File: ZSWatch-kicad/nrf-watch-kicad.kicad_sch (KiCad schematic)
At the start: 90 parts, among them IC1 TLV840MAPL36DBVRQ1, IC2 XC9265C181MR-G, IC3 TPS61023DRLT, IC4 MAX30101EFD+T, M1 Vibrator DC Motor, Q1 DMP2045U-7, Q2 SS8050-G, U1 MAX1811ESA+, U2 DMC2400UV-7, U3 LIS2DS12TR, U4 MX25R6435FZNIL0, U5 u-blox ANNA-B402, U6 DRV2603RUNT, U7 XC9265A331MR-G, U8 TXB0104QRUTRQ1, U9 GC9A01

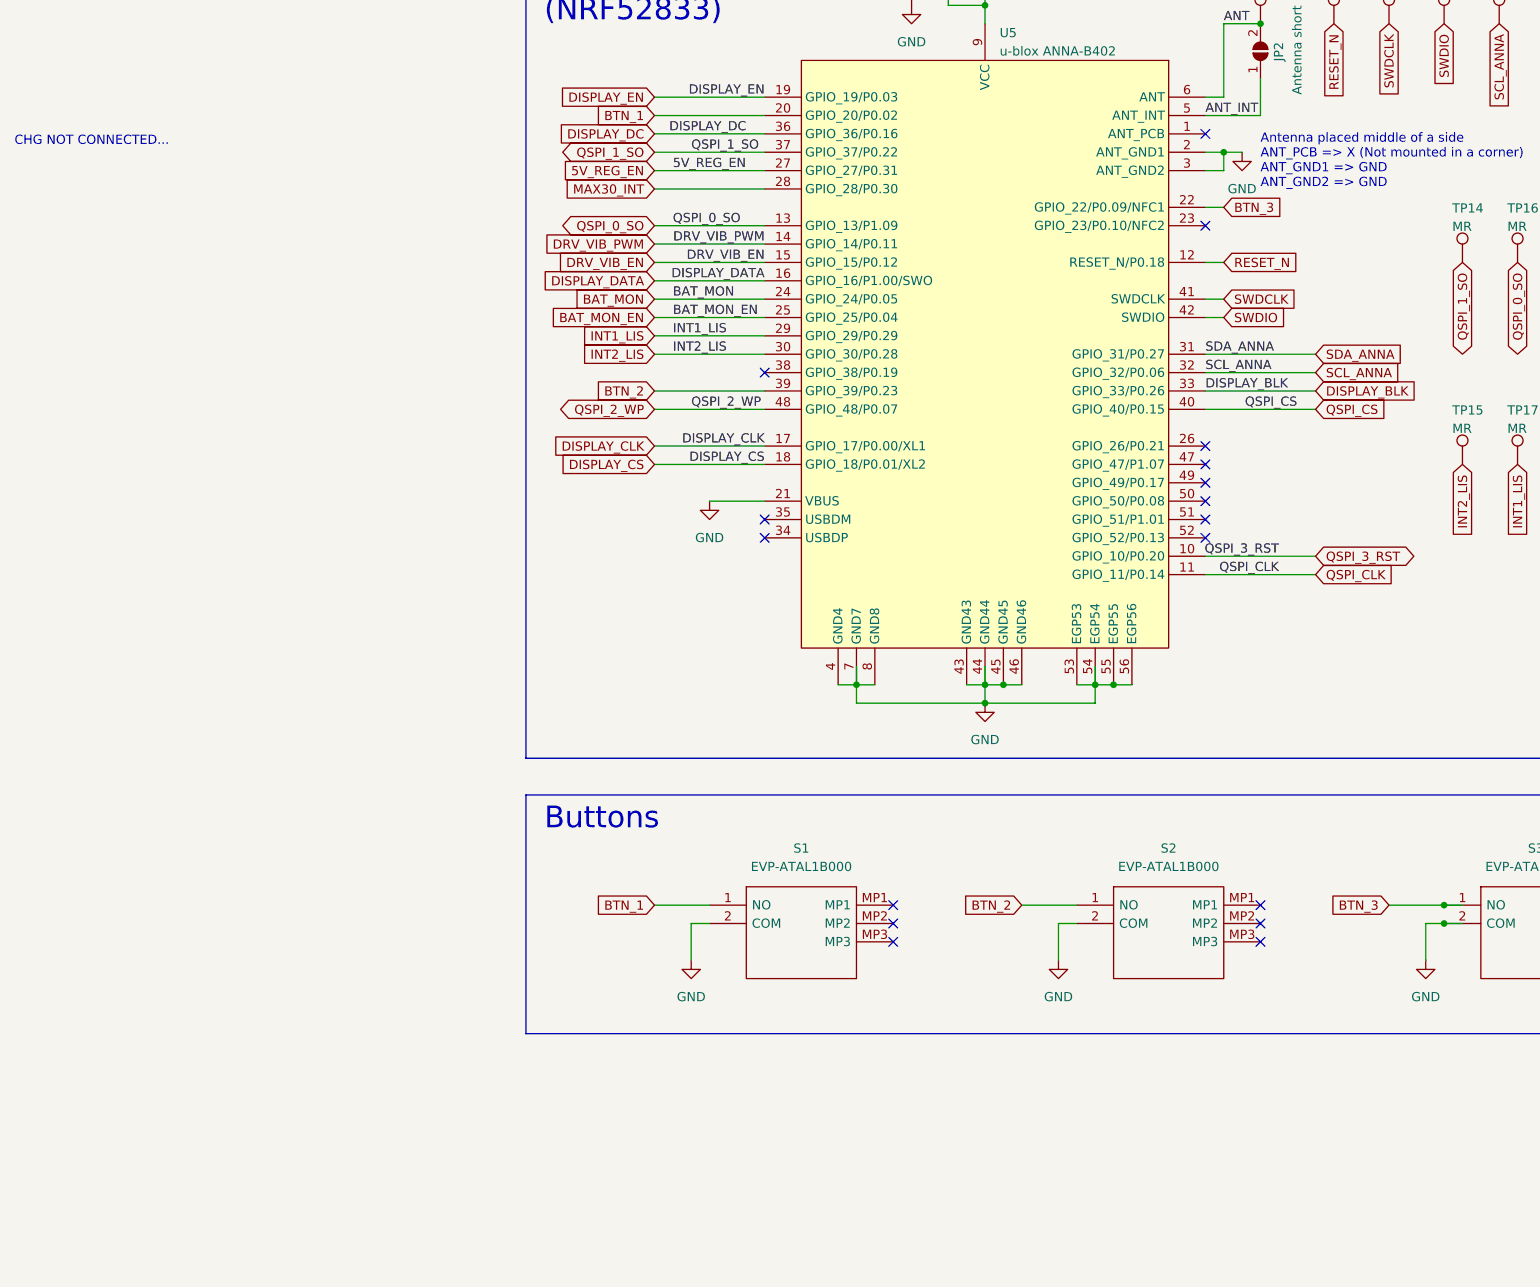
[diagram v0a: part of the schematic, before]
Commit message: Remove unused parts from v1.
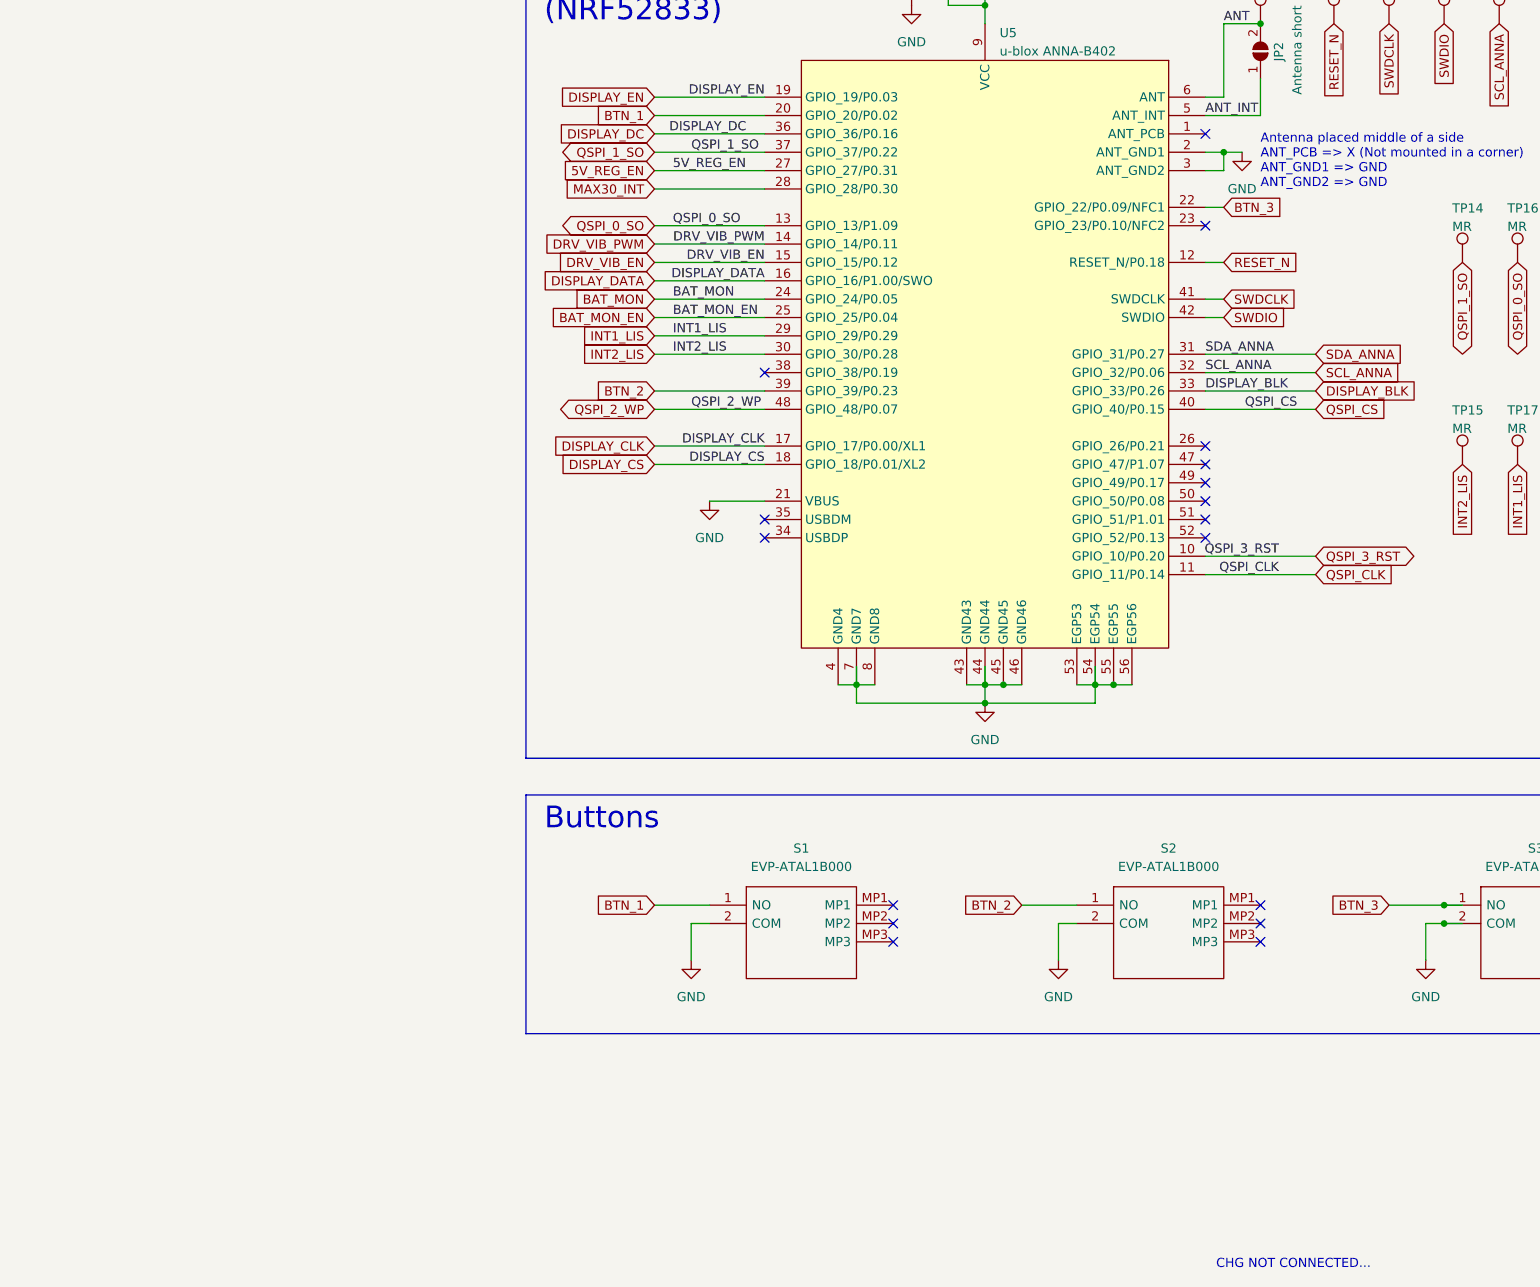
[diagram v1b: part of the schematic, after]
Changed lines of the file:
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@@
     (effects (font (size 1.27 1.27)) (justify left bottom))
   )
-  (text "CHG NOT CONNECTED..." (at -55.5092 197.3675 0)
+  (text "CHG NOT CONNECTED..." (at 110.7074 352.7166 0)
     (effects (font (size 1.27 1.27)) (justify left bottom))
   )
